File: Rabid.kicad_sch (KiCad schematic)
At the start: 223 parts, among them J1 USB Connector, J3 GPIO Debug Header, SW1 Esc, SW10 A, SW100 Unused, SW101 Unused, SW102 →, SW103 BootSel Switch, SW104 Reset Switch, SW11 Z, SW12 LMeta, SW13 F1, SW14 2, SW15 W, SW16 S, SW17 X, SW18 LAlt, SW19 F2, SW2 Tilde, SW20 3, SW21 E, SW22 D, SW23 C, SW24 Unused, SW25 F3, SW26 4, SW27 R, SW28 F, SW29 V, SW3 Tab, SW30 Unused, SW31 F4, SW32 5, SW33 T, SW34 G, SW35 B, SW36 Unused, SW37 F5, SW38 6, SW39 Y, SW4 CapsLk, SW40 H, SW41 N, SW42 Space, SW43 F6, SW44 7, SW45 U, SW46 J, SW47 M, SW48 Unused, SW49 F7, SW5 LShift, SW50 8, SW51 I, SW52 K, SW53 ,, SW54 Unused, SW55 F8, SW56 9, SW57 O, SW58 L, SW59 ., SW6 LCtrl, SW60 Unused, SW61 F9, SW62 0, SW63 P, SW64 ;, SW65 /, SW66 AltGr, SW67 F10, SW68 -, SW69 [, SW7 Unused, SW70 ", SW71 RShift, SW72 RMeta, SW73 F11, SW74 =, SW75 ]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

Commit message: Change all mounting holes to 8.2mm diameter.
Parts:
- H1, H2, H3, H4, H5, H7: value MountingHole.35in -> MountingHole_8.2mm; footprint RabidKeyboard:MountingHole_.35in -> RabidKeyboard:MountingHole_8.2mm
- H6: value MountingHole.25in -> MountingHole_8.2mm; footprint RabidKeyboard:MountingHole_.25in -> RabidKeyboard:MountingHole_8.2mm
- H8: value MountingHole4mm -> MountingHole_8.2mm
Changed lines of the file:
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@@
       (effects (font (size 1.27 1.27)) (justify left))
     )
-    (property "Value" "MountingHole.35in" (id 1) (at 280.67 275.5899 0)
+    (property "Value" "MountingHole_8.2mm" (id 1) (at 280.67 275.5899 0)
       (effects (font (size 1.27 1.27)) (justify left))
     )
-    (property "Footprint" "RabidKeyboard:MountingHole_.35in" (id 2) (at 278.13 274.32 0)
+    (property "Footprint" "RabidKeyboard:MountingHole_8.2mm" (id 2) (at 278.13 274.32 0)
       (effects (font (size 1.27 1.27)) hide)
     )
@@
       (effects (font (size 1.27 1.27)) (justify left))
     )
-    (property "Value" "MountingHole.35in" (id 1) (at 256.54 275.5899 0)
+    (property "Value" "MountingHole_8.2mm" (id 1) (at 256.54 275.5899 0)
       (effects (font (size 1.27 1.27)) (justify left))
     )
-    (property "Footprint" "RabidKeyboard:MountingHole_.35in" (id 2) (at 254 274.32 0)
+    (property "Footprint" "RabidKeyboard:MountingHole_8.2mm" (id 2) (at 254 274.32 0)
       (effects (font (size 1.27 1.27)) hide)
     )
@@
       (effects (font (size 1.27 1.27)) (justify left))
     )
-    (property "Value" "MountingHole.35in" (id 1) (at 256.54 281.9399 0)
+    (property "Value" "MountingHole_8.2mm" (id 1) (at 256.54 281.9399 0)
       (effects (font (size 1.27 1.27)) (justify left))
     )
-    (property "Footprint" "RabidKeyboard:MountingHole_.35in" (id 2) (at 254 280.67 0)
+    (property "Footprint" "RabidKeyboard:MountingHole_8.2mm" (id 2) (at 254 280.67 0)
       (effects (font (size 1.27 1.27)) hide)
     )
@@
       (effects (font (size 1.27 1.27)) (justify left))
     )
-    (property "Value" "MountingHole.35in" (id 1) (at 280.67 262.8899 0)
+    (property "Value" "MountingHole_8.2mm" (id 1) (at 280.67 262.8899 0)
       (effects (font (size 1.27 1.27)) (justify left))
     )
-    (property "Footprint" "RabidKeyboard:MountingHole_.35in" (id 2) (at 278.13 261.62 0)
+    (property "Footprint" "RabidKeyboard:MountingHole_8.2mm" (id 2) (at 278.13 261.62 0)
       (effects (font (size 1.27 1.27)) hide)
     )
@@
       (effects (font (size 1.27 1.27)) (justify left))
     )
-    (property "Value" "MountingHole.35in" (id 1) (at 256.54 262.8899 0)
+    (property "Value" "MountingHole_8.2mm" (id 1) (at 256.54 262.8899 0)
       (effects (font (size 1.27 1.27)) (justify left))
     )
-    (property "Footprint" "RabidKeyboard:MountingHole_.35in" (id 2) (at 254 261.62 0)
+    (property "Footprint" "RabidKeyboard:MountingHole_8.2mm" (id 2) (at 254 261.62 0)
       (effects (font (size 1.27 1.27)) hide)
     )
@@
       (effects (font (size 1.27 1.27)) (justify left))
     )
-    (property "Value" "MountingHole.35in" (id 1) (at 256.54 269.2399 0)
+    (property "Value" "MountingHole_8.2mm" (id 1) (at 256.54 269.2399 0)
       (effects (font (size 1.27 1.27)) (justify left))
     )
-    (property "Footprint" "RabidKeyboard:MountingHole_.35in" (id 2) (at 254 267.97 0)
+    (property "Footprint" "RabidKeyboard:MountingHole_8.2mm" (id 2) (at 254 267.97 0)
       (effects (font (size 1.27 1.27)) hide)
     )
@@
       (effects (font (size 1.27 1.27)) (justify left))
     )
-    (property "Value" "MountingHole.25in" (id 1) (at 280.67 269.2399 0)
+    (property "Value" "MountingHole_8.2mm" (id 1) (at 280.67 269.2399 0)
       (effects (font (size 1.27 1.27)) (justify left))
     )
-    (property "Footprint" "RabidKeyboard:MountingHole_.25in" (id 2) (at 278.13 267.97 0)
+    (property "Footprint" "RabidKeyboard:MountingHole_8.2mm" (id 2) (at 278.13 267.97 0)
       (effects (font (size 1.27 1.27)) hide)
     )
@@
       (effects (font (size 1.27 1.27)) (justify left))
     )
-    (property "Value" "MountingHole4mm" (id 1) (at 280.67 281.9399 0)
+    (property "Value" "MountingHole_8.2mm" (id 1) (at 280.67 281.9399 0)
       (effects (font (size 1.27 1.27)) (justify left))
     )
@@
     )
     (path "/7ab71991-2b35-4dfe-a3d1-e1d6a93c8aa2"
-      (reference "H1") (unit 1) (value "MountingHole.35in") (footprint "RabidKeyboard:MountingHole_.35in")
+      (reference "H1") (unit 1) (value "MountingHole_8.2mm") (footprint "RabidKeyboard:MountingHole_8.2mm")
     )
     (path "/84b27060-4b68-4266-a520-6b17d4002257"
-      (reference "H2") (unit 1) (value "MountingHole.35in") (footprint "RabidKeyboard:MountingHole_.35in")
+      (reference "H2") (unit 1) (value "MountingHole_8.2mm") (footprint "RabidKeyboard:MountingHole_8.2mm")
     )
     (path "/18a8f0d3-5ac8-4d2b-aaf1-8fd815948e6a"
-      (reference "H3") (unit 1) (value "MountingHole.35in") (footprint "RabidKeyboard:MountingHole_.35in")
+      (reference "H3") (unit 1) (value "MountingHole_8.2mm") (footprint "RabidKeyboard:MountingHole_8.2mm")
     )
     (path "/23a84009-b94e-4473-821b-756b9ff8be21"
-      (reference "H4") (unit 1) (value "MountingHole.35in") (footprint "RabidKeyboard:MountingHole_.35in")
+      (reference "H4") (unit 1) (value "MountingHole_8.2mm") (footprint "RabidKeyboard:MountingHole_8.2mm")
     )
     (path "/6a239d85-40cc-4822-a383-2dc31e36eed3"
-      (reference "H5") (unit 1) (value "MountingHole.35in") (footprint "RabidKeyboard:MountingHole_.35in")
+      (reference "H5") (unit 1) (value "MountingHole_8.2mm") (footprint "RabidKeyboard:MountingHole_8.2mm")
     )
     (path "/b0e52192-3ce8-4daa-8b02-fbc5aef0027e"
-      (reference "H6") (unit 1) (value "MountingHole.25in") (footprint "RabidKeyboard:MountingHole_.25in")
+      (reference "H6") (unit 1) (value "MountingHole_8.2mm") (footprint "RabidKeyboard:MountingHole_8.2mm")
     )
     (path "/02f4d47d-ab1d-4f2f-9935-90a7fb385495"
-      (reference "H7") (unit 1) (value "MountingHole.35in") (footprint "RabidKeyboard:MountingHole_.35in")
+      (reference "H7") (unit 1) (value "MountingHole_8.2mm") (footprint "RabidKeyboard:MountingHole_8.2mm")
     )
     (path "/daf18d95-a29d-445d-9e50-3ca1c1c87614"
-      (reference "H8") (unit 1) (value "MountingHole4mm") (footprint "MountingHole:MountingHole_4mm")
+      (reference "H8") (unit 1) (value "MountingHole_8.2mm") (footprint "MountingHole:MountingHole_4mm")
     )
     (path "/bbea82d0-8c64-4c6e-81d8-7d16f5942bd3"

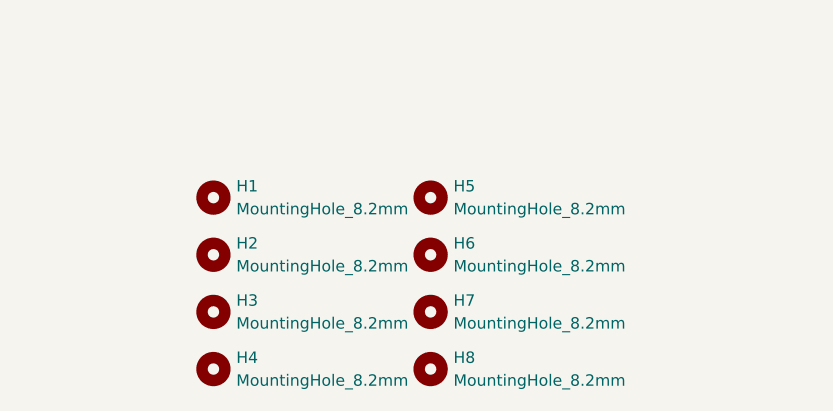
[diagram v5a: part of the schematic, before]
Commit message: Change DRC rules to match JLCPCB.
 - Fixed some DRC errors by adjusting tolerances.
    (Seems Kicad has some rounding error in differential pair gap DRC?)
 - Add "JLCJLCJLCJLC" to silkscreen for JLCPCB to replace with order number.
 - Slight adjustments to mounting holes.
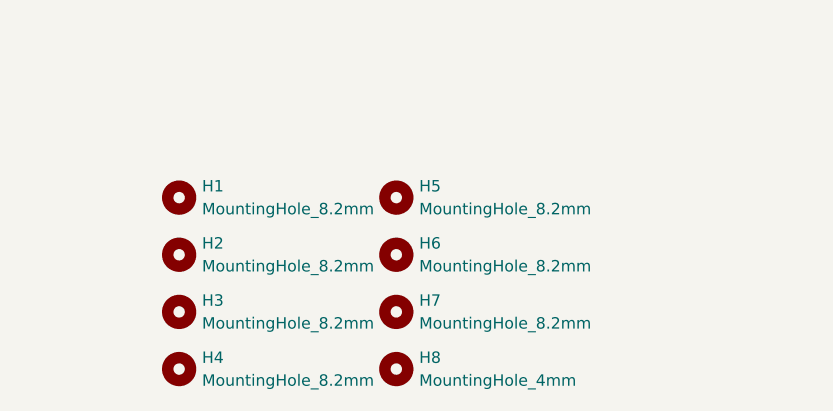
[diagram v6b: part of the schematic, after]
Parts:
- H8: value MountingHole_8.2mm -> MountingHole_4mm; footprint MountingHole:MountingHole_4mm -> RabidKeyboard:MountingHole_4mm
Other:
- moved on the sheet: H1, H2, H3, H4, H5, H6, H7, H8
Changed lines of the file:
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@@
     (pin "2")
   )
-  (symbol (lib_id "Mechanical:MountingHole") (at 278.13 274.32 0) (unit 1)
+  (symbol (lib_id "Mechanical:MountingHole") (at 274.32 274.32 0) (unit 1)
     (in_bom yes) (on_board yes) (fields_autoplaced)
-    (property "Reference" "H7" (id 0) (at 280.67 273.0499 0)
+    (property "Reference" "H7" (id 0) (at 276.86 273.0499 0)
       (effects (font (size 1.27 1.27)) (justify left))
     )
-    (property "Value" "MountingHole_8.2mm" (id 1) (at 280.67 275.5899 0)
+    (property "Value" "MountingHole_8.2mm" (id 1) (at 276.86 275.5899 0)
       (effects (font (size 1.27 1.27)) (justify left))
     )
-    (property "Footprint" "RabidKeyboard:MountingHole_8.2mm" (id 2) (at 278.13 274.32 0)
+    (property "Footprint" "RabidKeyboard:MountingHole_8.2mm" (id 2) (at 274.32 274.32 0)
       (effects (font (size 1.27 1.27)) hide)
     )
-    (property "Datasheet" "~" (id 3) (at 278.13 274.32 0)
+    (property "Datasheet" "~" (id 3) (at 274.32 274.32 0)
       (effects (font (size 1.27 1.27)) hide)
     )
@@
     (pin "2")
   )
-  (symbol (lib_id "Mechanical:MountingHole") (at 254 274.32 0) (unit 1)
+  (symbol (lib_id "Mechanical:MountingHole") (at 250.19 274.32 0) (unit 1)
     (in_bom yes) (on_board yes) (fields_autoplaced)
-    (property "Reference" "H3" (id 0) (at 256.54 273.0499 0)
+    (property "Reference" "H3" (id 0) (at 252.73 273.0499 0)
       (effects (font (size 1.27 1.27)) (justify left))
     )
-    (property "Value" "MountingHole_8.2mm" (id 1) (at 256.54 275.5899 0)
+    (property "Value" "MountingHole_8.2mm" (id 1) (at 252.73 275.5899 0)
       (effects (font (size 1.27 1.27)) (justify left))
     )
-    (property "Footprint" "RabidKeyboard:MountingHole_8.2mm" (id 2) (at 254 274.32 0)
+    (property "Footprint" "RabidKeyboard:MountingHole_8.2mm" (id 2) (at 250.19 274.32 0)
       (effects (font (size 1.27 1.27)) hide)
     )
-    (property "Datasheet" "~" (id 3) (at 254 274.32 0)
+    (property "Datasheet" "~" (id 3) (at 250.19 274.32 0)
       (effects (font (size 1.27 1.27)) hide)
     )
@@
     (pin "2")
   )
-  (symbol (lib_id "Mechanical:MountingHole") (at 254 280.67 0) (unit 1)
+  (symbol (lib_id "Mechanical:MountingHole") (at 250.19 280.67 0) (unit 1)
     (in_bom yes) (on_board yes) (fields_autoplaced)
-    (property "Reference" "H4" (id 0) (at 256.54 279.3999 0)
+    (property "Reference" "H4" (id 0) (at 252.73 279.3999 0)
       (effects (font (size 1.27 1.27)) (justify left))
     )
-    (property "Value" "MountingHole_8.2mm" (id 1) (at 256.54 281.9399 0)
+    (property "Value" "MountingHole_8.2mm" (id 1) (at 252.73 281.9399 0)
       (effects (font (size 1.27 1.27)) (justify left))
     )
-    (property "Footprint" "RabidKeyboard:MountingHole_8.2mm" (id 2) (at 254 280.67 0)
+    (property "Footprint" "RabidKeyboard:MountingHole_8.2mm" (id 2) (at 250.19 280.67 0)
       (effects (font (size 1.27 1.27)) hide)
     )
-    (property "Datasheet" "~" (id 3) (at 254 280.67 0)
+    (property "Datasheet" "~" (id 3) (at 250.19 280.67 0)
       (effects (font (size 1.27 1.27)) hide)
     )
@@
     (pin "2")
   )
-  (symbol (lib_id "Mechanical:MountingHole") (at 278.13 261.62 0) (unit 1)
+  (symbol (lib_id "Mechanical:MountingHole") (at 274.32 261.62 0) (unit 1)
     (in_bom yes) (on_board yes) (fields_autoplaced)
-    (property "Reference" "H5" (id 0) (at 280.67 260.3499 0)
+    (property "Reference" "H5" (id 0) (at 276.86 260.3499 0)
       (effects (font (size 1.27 1.27)) (justify left))
     )
-    (property "Value" "MountingHole_8.2mm" (id 1) (at 280.67 262.8899 0)
+    (property "Value" "MountingHole_8.2mm" (id 1) (at 276.86 262.8899 0)
       (effects (font (size 1.27 1.27)) (justify left))
     )
-    (property "Footprint" "RabidKeyboard:MountingHole_8.2mm" (id 2) (at 278.13 261.62 0)
+    (property "Footprint" "RabidKeyboard:MountingHole_8.2mm" (id 2) (at 274.32 261.62 0)
       (effects (font (size 1.27 1.27)) hide)
     )
-    (property "Datasheet" "~" (id 3) (at 278.13 261.62 0)
+    (property "Datasheet" "~" (id 3) (at 274.32 261.62 0)
       (effects (font (size 1.27 1.27)) hide)
     )
@@
     (pin "2")
   )
-  (symbol (lib_id "Mechanical:MountingHole") (at 254 261.62 0) (unit 1)
+  (symbol (lib_id "Mechanical:MountingHole") (at 250.19 261.62 0) (unit 1)
     (in_bom yes) (on_board yes) (fields_autoplaced)
-    (property "Reference" "H1" (id 0) (at 256.54 260.3499 0)
+    (property "Reference" "H1" (id 0) (at 252.73 260.3499 0)
       (effects (font (size 1.27 1.27)) (justify left))
     )
-    (property "Value" "MountingHole_8.2mm" (id 1) (at 256.54 262.8899 0)
+    (property "Value" "MountingHole_8.2mm" (id 1) (at 252.73 262.8899 0)
       (effects (font (size 1.27 1.27)) (justify left))
     )
-    (property "Footprint" "RabidKeyboard:MountingHole_8.2mm" (id 2) (at 254 261.62 0)
+    (property "Footprint" "RabidKeyboard:MountingHole_8.2mm" (id 2) (at 250.19 261.62 0)
       (effects (font (size 1.27 1.27)) hide)
     )
-    (property "Datasheet" "~" (id 3) (at 254 261.62 0)
+    (property "Datasheet" "~" (id 3) (at 250.19 261.62 0)
       (effects (font (size 1.27 1.27)) hide)
     )
@@
     (pin "2")
   )
-  (symbol (lib_id "Mechanical:MountingHole") (at 254 267.97 0) (unit 1)
+  (symbol (lib_id "Mechanical:MountingHole") (at 250.19 267.97 0) (unit 1)
     (in_bom yes) (on_board yes) (fields_autoplaced)
-    (property "Reference" "H2" (id 0) (at 256.54 266.6999 0)
+    (property "Reference" "H2" (id 0) (at 252.73 266.6999 0)
       (effects (font (size 1.27 1.27)) (justify left))
     )
-    (property "Value" "MountingHole_8.2mm" (id 1) (at 256.54 269.2399 0)
+    (property "Value" "MountingHole_8.2mm" (id 1) (at 252.73 269.2399 0)
       (effects (font (size 1.27 1.27)) (justify left))
     )
-    (property "Footprint" "RabidKeyboard:MountingHole_8.2mm" (id 2) (at 254 267.97 0)
+    (property "Footprint" "RabidKeyboard:MountingHole_8.2mm" (id 2) (at 250.19 267.97 0)
       (effects (font (size 1.27 1.27)) hide)
     )
-    (property "Datasheet" "~" (id 3) (at 254 267.97 0)
+    (property "Datasheet" "~" (id 3) (at 250.19 267.97 0)
       (effects (font (size 1.27 1.27)) hide)
     )
@@
     (pin "2")
   )
-  (symbol (lib_id "Mechanical:MountingHole") (at 278.13 267.97 0) (unit 1)
+  (symbol (lib_id "Mechanical:MountingHole") (at 274.32 267.97 0) (unit 1)
     (in_bom yes) (on_board yes)
-    (property "Reference" "H6" (id 0) (at 280.67 266.6999 0)
+    (property "Reference" "H6" (id 0) (at 276.86 266.6999 0)
       (effects (font (size 1.27 1.27)) (justify left))
     )
-    (property "Value" "MountingHole_8.2mm" (id 1) (at 280.67 269.2399 0)
+    (property "Value" "MountingHole_8.2mm" (id 1) (at 276.86 269.2399 0)
       (effects (font (size 1.27 1.27)) (justify left))
     )
-    (property "Footprint" "RabidKeyboard:MountingHole_8.2mm" (id 2) (at 278.13 267.97 0)
+    (property "Footprint" "RabidKeyboard:MountingHole_8.2mm" (id 2) (at 274.32 267.97 0)
       (effects (font (size 1.27 1.27)) hide)
     )
-    (property "Datasheet" "~" (id 3) (at 278.13 267.97 0)
+    (property "Datasheet" "~" (id 3) (at 274.32 267.97 0)
       (effects (font (size 1.27 1.27)) hide)
     )
@@
     (pin "2")
   )
-  (symbol (lib_id "Mechanical:MountingHole") (at 278.13 280.67 0) (unit 1)
+  (symbol (lib_id "Mechanical:MountingHole") (at 274.32 280.67 0) (unit 1)
     (in_bom yes) (on_board yes) (fields_autoplaced)
-    (property "Reference" "H8" (id 0) (at 280.67 279.3999 0)
+    (property "Reference" "H8" (id 0) (at 276.86 279.3999 0)
       (effects (font (size 1.27 1.27)) (justify left))
     )
-    (property "Value" "MountingHole_8.2mm" (id 1) (at 280.67 281.9399 0)
+    (property "Value" "MountingHole_4mm" (id 1) (at 276.86 281.9399 0)
       (effects (font (size 1.27 1.27)) (justify left))
     )
-    (property "Footprint" "MountingHole:MountingHole_4mm" (id 2) (at 278.13 280.67 0)
+    (property "Footprint" "RabidKeyboard:MountingHole_4mm" (id 2) (at 274.32 280.67 0)
       (effects (font (size 1.27 1.27)) hide)
     )
-    (property "Datasheet" "~" (id 3) (at 278.13 280.67 0)
+    (property "Datasheet" "~" (id 3) (at 274.32 280.67 0)
       (effects (font (size 1.27 1.27)) hide)
     )
@@
     )
     (path "/daf18d95-a29d-445d-9e50-3ca1c1c87614"
-      (reference "H8") (unit 1) (value "MountingHole_8.2mm") (footprint "MountingHole:MountingHole_4mm")
+      (reference "H8") (unit 1) (value "MountingHole_4mm") (footprint "RabidKeyboard:MountingHole_4mm")
     )
     (path "/bbea82d0-8c64-4c6e-81d8-7d16f5942bd3"

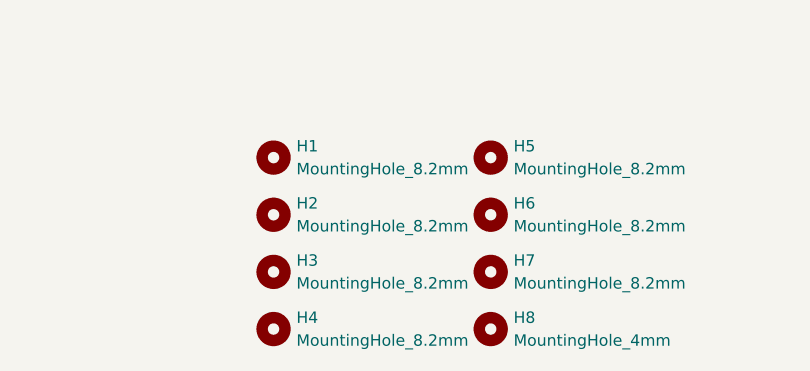
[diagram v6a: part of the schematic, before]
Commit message: Make Filco mounting hole smaller.
 - Add logo under spacebar.
 - Change PCB colour to black.
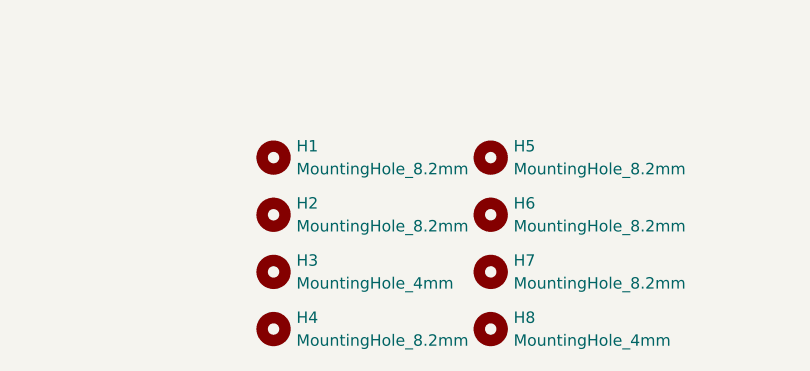
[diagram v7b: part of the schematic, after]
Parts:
- H3: value MountingHole_8.2mm -> MountingHole_4mm; footprint RabidKeyboard:MountingHole_8.2mm -> RabidKeyboard:MountingHole_4mm
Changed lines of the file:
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@@
       (effects (font (size 1.27 1.27)) (justify left))
     )
-    (property "Value" "MountingHole_8.2mm" (id 1) (at 252.73 275.5899 0)
+    (property "Value" "MountingHole_4mm" (id 1) (at 252.73 275.5899 0)
       (effects (font (size 1.27 1.27)) (justify left))
     )
-    (property "Footprint" "RabidKeyboard:MountingHole_8.2mm" (id 2) (at 250.19 274.32 0)
+    (property "Footprint" "RabidKeyboard:MountingHole_4mm" (id 2) (at 250.19 274.32 0)
       (effects (font (size 1.27 1.27)) hide)
     )
@@
     )
     (path "/18a8f0d3-5ac8-4d2b-aaf1-8fd815948e6a"
-      (reference "H3") (unit 1) (value "MountingHole_8.2mm") (footprint "RabidKeyboard:MountingHole_8.2mm")
+      (reference "H3") (unit 1) (value "MountingHole_4mm") (footprint "RabidKeyboard:MountingHole_4mm")
     )
     (path "/23a84009-b94e-4473-821b-756b9ff8be21"
